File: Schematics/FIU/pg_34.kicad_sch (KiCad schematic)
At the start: 17 parts, among them U3501 F04, U3502 F04, U3503 F04, U3504 F04, U3505 F04, U3506 F04, U3507 F283, U3508 F02, U3509 F02, U3510 F02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

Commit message: Align to grid
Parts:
- removed U3501, U3502, U3503, U3504, U3505, U3506, U3512, U3514: F04, symbol r1000:F04
- removed U3507: F283, symbol r1000:F283
- removed U3508, U3509, U3510, U3511, U3517: F02, symbol r1000:F02
- removed U3513: F181, symbol r1000:F181
- removed U3515, U3516: F157, symbol r1000:F157
- added U (x2): (no value), symbol r1000:F157
- added U (x8): (no value), symbol r1000:F04
- added U (x5): (no value), symbol r1000:F02
- added U: (no value), symbol r1000:F181
- added U: (no value), symbol r1000:F283
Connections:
- net EBIT0: now also U.11 (Y1)
- net EBIT1: now also U.10 (Y2)
- net EBIT2: now also U.9 (Y3)
- net EBIT~3: now also U.3 (Q)
- net EBIT~4: now also U.3 (Q)
- net EBIT~5: now also U.3 (Q)
- net EBIT~6: now also U.3 (Q)
- net LENGTH_ONE0: now also U.1 (D0), U.22 (B2)
- net LENGTH_ONE1: now also U.1 (B3), U.1 (D0)
- net LENGTH_ONE2: now also U.1 (D0), U.11 (B0)
- net LENGTH_ONE3: now also U.1 (D0), U.15 (B1)
- net LENGTH_ONE4: now also U.1 (D0), U.2 (B2)
- net LENGTH_ONE5: now also U.1 (D0), U.6 (B3)
- net LENGTH_ONE~0: now also U.11 (A2), U.2 (Q)
- net LENGTH_ONE~1: now also U.14 (A3), U.2 (Q)
- net LENGTH_ONE~2: now also U.2 (A0), U.2 (Q)
- net LENGTH_ONE~3: now also U.2 (Q), U.5 (A1)
- net LENGTH_ONE~4: now also U.11 (A2), U.2 (Q)
- net LENGTH_ONE~5: now also U.14 (A3), U.2 (Q)
- net OFFSET0.B0: now also U.21 (A1), U.3 (B0), U.6 (B1)
- net OFFSET1: now also U.10 (B2), U.23 (A2)
- net OFFSET2: now also U.13 (B3), U.2 (A3)
- net OFFSET3: now also U.12 (A0), U.3 (B0)
- net OFFSET4: now also U.14 (A1), U.6 (B1)
- net OFFSET5: now also U.10 (B2), U.3 (A2)
- net OFFSET6: now also U.13 (B3), U.5 (A3)
- net OP_SEL0: now also U.1 (S), U.1 (S), U.2 (D1)
- net OP_SEL1: now also U.1 (D0), U.6 (S3)
- net OP_SEL~1: now also U.1 (D0), U.1 (D0), U.1 (D0), U.2 (D1), U.2 (D1), U.2 (Q), U.4 (S1), U.8 (M)
- net PD: now also U.18 (B0), U.19 (A0), U.20 (B1), U.5 (S2), U.7 (CI)
- net PU: now also U.2 (A0), U.3 (S0), U.5 (A1)
- net SBIT0.B0: now also U.4 (Y0)
- net SBIT0.B1: now also U.7 (Y1)
- net SBIT1: now also U.9 (Y2)
- net SBIT2: now also U.12 (Y3)
- net SBIT3: now also U.4 (Y0)
- net SBIT4: now also U.7 (Y1)
- net SBIT5: now also U.9 (Y2)
- net SBIT6: now also U.12 (Y3)
- new net: U.15 (E), U.15 (E), U.3 (Q)
- new net: U.1 (D0), U.4 (Y3)
- new net: U.2 (Q), U.7 (CI)
- new net: U.13 (Y1), U.2 (D1)
- new net: U.10 (Y0), U.2 (D1)
- new net: U.1 (D0), U.9 (CO)
- new net: U.1 (D0), U.1 (Y2)

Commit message: FIU: dedup, clocks, dfsm
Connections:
- net OFFSET0.B0 renamed OFFSET0
- net SBIT0.B0: no longer names the net of U.4 (Y0)
- net SBIT0.B1 renamed SBIT0
- no-connect marks 5 -> 6
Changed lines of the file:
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@@
   (no_connect (at 436.88 149.86))
   (no_connect (at 436.88 144.78))
+  (no_connect (at 187.96 96.52))
   (bus_entry (at 520.7 251.46) (size -2.54 2.54)
     (stroke (width 0) (type default))
@@
     (stroke (width 0) (type default))
   )
+  (bus_entry (at 251.46 104.14) (size -2.54 2.54)
+    (stroke (width 0) (type default))
+  )
   (bus_entry (at 81.28 218.44) (size 2.54 2.54)
     (stroke (width 0) (type default))
@@
     (stroke (width 0) (type default))
   )
-  (bus (pts (xy 251.46 111.76) (xy 259.08 111.76))
+  (bus (pts (xy 251.46 101.6) (xy 259.08 101.6))
     (stroke (width 0) (type default))
   )
@@
     (stroke (width 0) (type default))
   )
-  (wire (pts (xy 187.96 96.52) (xy 248.92 96.52))
-    (stroke (width 0) (type default))
-  )
   (bus (pts (xy 73.66 327.66) (xy 73.66 342.9))
     (stroke (width 0) (type default))
@@
     (stroke (width 0) (type default))
   )
-  (bus (pts (xy 251.46 111.76) (xy 251.46 114.3))
+  (bus (pts (xy 251.46 101.6) (xy 251.46 104.14))
     (stroke (width 0) (type default))
   )
@@
     (stroke (width 0) (type default))
   )
+  (bus (pts (xy 251.46 104.14) (xy 251.46 114.3))
+    (stroke (width 0) (type default))
+  )
   (wire (pts (xy 327.66 165.1) (xy 388.62 165.1))
     (stroke (width 0) (type default))
@@
     (effects (font (size 2.54 2.54)) (justify left bottom))
   )
+  (label "SBIT0" (at 215.9 106.68 0) (fields_autoplaced)
+    (effects (font (size 2.54 2.54)) (justify left bottom))
+  )
   (label "LENGTH_ONE~2" (at 137.16 314.96 0) (fields_autoplaced)
     (effects (font (size 2.54 2.54)) (justify left bottom))
   )
-  (label "OFFSET0.B0" (at 337.82 139.7 0) (fields_autoplaced)
+  (label "OFFSET0" (at 337.82 139.7 0) (fields_autoplaced)
     (effects (font (size 2.54 2.54)) (justify left bottom))
   )
@@
     )
   )
-  (global_label "SBIT0.B0" (shape output) (at 248.92 96.52 0) (fields_autoplaced)
-    (effects (font (size 2.54 2.54)) (justify left))
-    (property "Intersheet References" "${INTERSHEET_REFS}" (id 0) (at 270.4374 96.3613 0)
-      (effects (font (size 1.905 1.905)) (justify left))
-    )
-  )
-  (global_label "OFFSET0.B0" (shape input) (at 68.58 119.38 180) (fields_autoplaced)
+  (global_label "OFFSET0" (shape input) (at 68.58 119.38 180) (fields_autoplaced)
     (effects (font (size 2.54 2.54)) (justify right))
     (property "Intersheet References" "${INTERSHEET_REFS}" (id 0) (at 41.4988 119.2213 0)
       (effects (font (size 1.905 1.905)) (justify right))
-    )
-  )
-  (global_label "SBIT0.B1" (shape output) (at 248.92 106.68 0) (fields_autoplaced)
-    (effects (font (size 2.54 2.54)) (justify left))
-    (property "Intersheet References" "${INTERSHEET_REFS}" (id 0) (at 270.4374 106.5213 0)
-      (effects (font (size 1.905 1.905)) (justify left))
     )
   )
@@
     )
   )
-  (global_label "SBIT[1..6]" (shape output) (at 259.08 111.76 0) (fields_autoplaced)
+  (global_label "SBIT[0..6]" (shape output) (at 259.08 101.6 0) (fields_autoplaced)
     (effects (font (size 2.54 2.54)) (justify left))
-    (property "Intersheet References" "${INTERSHEET_REFS}" (id 0) (at 282.6536 111.6013 0)
+    (property "Intersheet References" "${INTERSHEET_REFS}" (id 0) (at 283.3202 101.6 0)
       (effects (font (size 1.905 1.905)) (justify left))
     )

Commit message: FIU: tested to 6.07s (rc019)
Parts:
- removed U (x2): (no value), symbol r1000:F157
- added U: XMUX7, symbol r1000:XMUX7
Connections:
- net LENGTH_ONE~0: now also U.3 (A1)
- net LENGTH_ONE~1: now also U.5 (A2)
- net LENGTH_ONE~2: now also U.7 (A3)
- net LENGTH_ONE~3: now also U.9 (A4)
- net LENGTH_ONE~4: now also U.10 (A5)
- net LENGTH_ONE~5: now also U.11 (A6)
- net OFFSET0: now also U.12 (B0)
- net OFFSET1: now also U.14 (B1)
- net OFFSET2: now also U.16 (B2)
- net OFFSET3: now also U.18 (B3)
- net OFFSET4: now also U.20 (B4)
- net OFFSET5: now also U.22 (B5)
- net OFFSET6: now also U.24 (B6)
- net OP_SEL0: now also U.4 (S)
- net PD: now also U.8 (OE)
- net PU: now also U.1 (A0)
- net SBIT0: now also U.13 (Y0)
- net SBIT1: now also U.15 (Y1)
- net SBIT2: now also U.17 (Y2)
- net SBIT3: now also U.19 (Y3)
- net SBIT4: now also U.21 (Y4)
- net SBIT5: now also U.23 (Y5)
- net SBIT6: now also U.25 (Y6)
- net at U.3 (Q): now also U.6 (E)

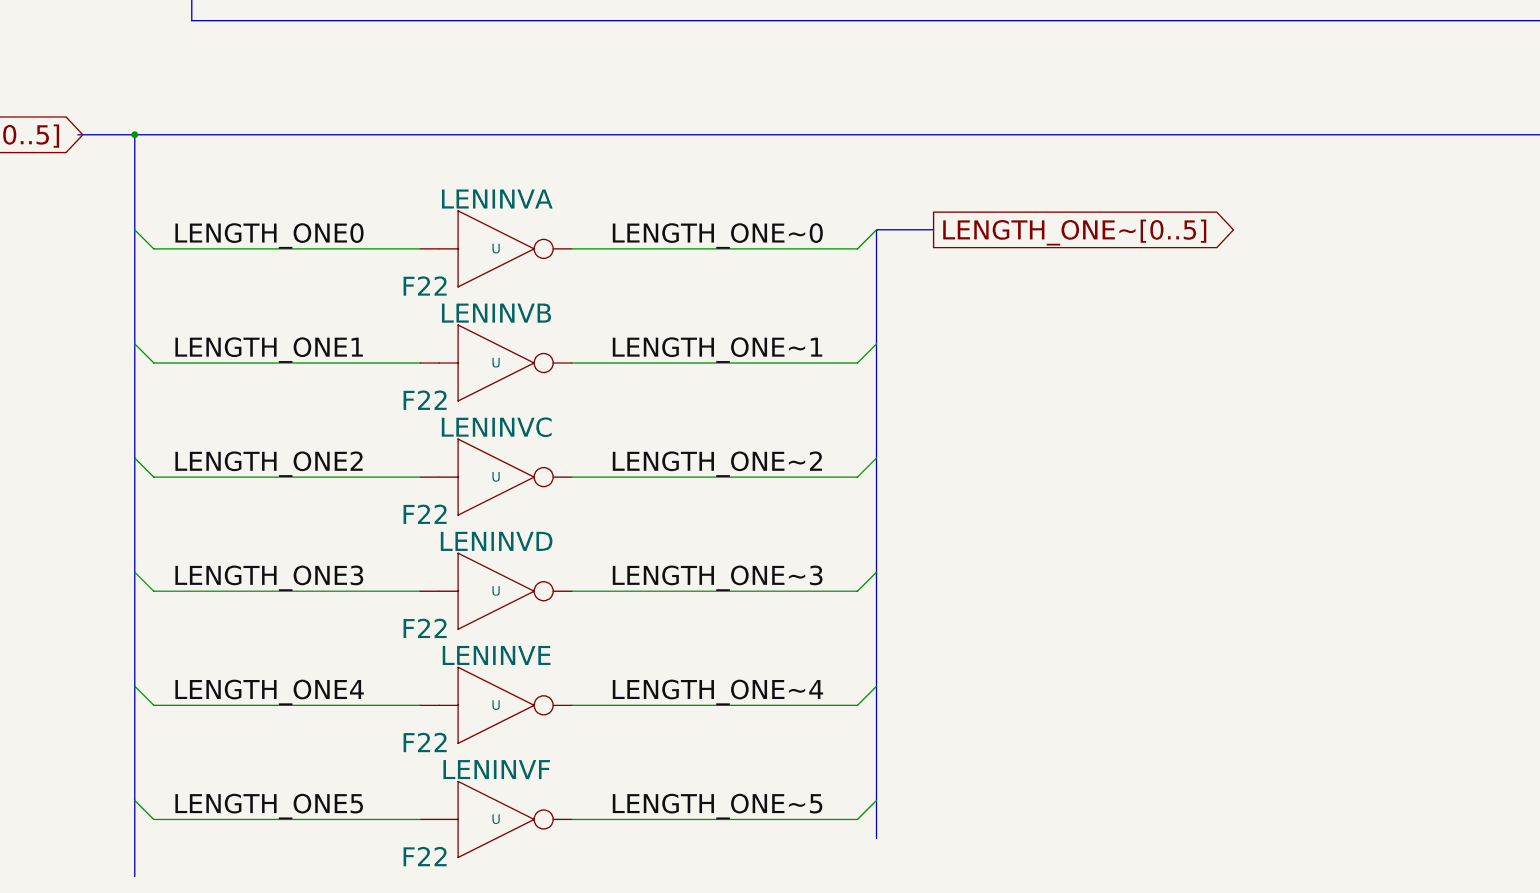
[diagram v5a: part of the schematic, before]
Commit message: FIU tested to 21.22 seconds (rm089)
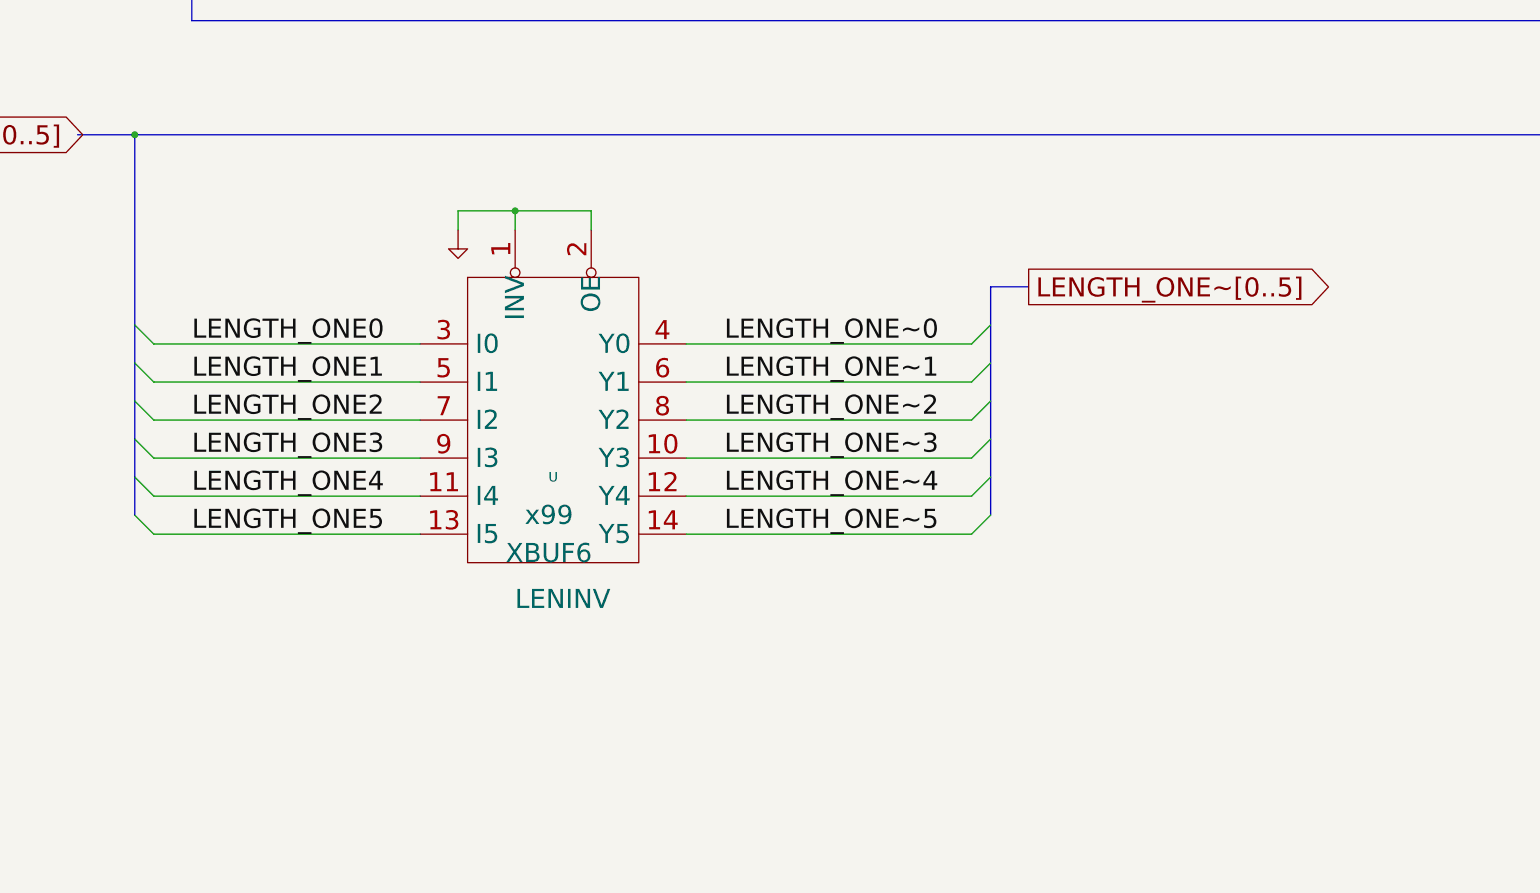
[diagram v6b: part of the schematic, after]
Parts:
- removed U (x6): (no value), symbol r1000:F04
- added U: XBUF6, symbol r1000:XBUF6
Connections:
- net LENGTH_ONE0: now also U.3 (I0)
- net LENGTH_ONE1: now also U.5 (I1)
- net LENGTH_ONE2: now also U.7 (I2)
- net LENGTH_ONE3: now also U.9 (I3)
- net LENGTH_ONE4: now also U.11 (I4)
- net LENGTH_ONE5: now also U.13 (I5)
- net LENGTH_ONE~0: now also U.4 (Y0)
- net LENGTH_ONE~1: now also U.6 (Y1)
- net LENGTH_ONE~2: now also U.8 (Y2)
- net LENGTH_ONE~3: now also U.10 (Y3)
- net LENGTH_ONE~4: now also U.12 (Y4)
- net LENGTH_ONE~5: now also U.14 (Y5)
- net PD: now also U.1 (INV), U.2 (OE)

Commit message: Eliminate empty pages
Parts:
- U3507: renamed from U; value (none) -> F283
- U3508, U3509, U3510, U3511, U3517: renamed from U; value (none) -> F02
- U3512, U3514: renamed from U; value (none) -> F04
- U3513: renamed from U; value (none) -> F181
- renumbered U to U82, U to U84

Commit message: Schematics for run rr026
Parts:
- added U3401: F02, symbol r1000:F02
- added U80: XADD8, symbol r1000:XADD8
- added U81: XMUX6, symbol r1000:XMUX6
- added U83: XSUB8, symbol r1000:XSUB8
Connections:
- net LENGTH_ONE0: now also U80.15 (B2)
- net LENGTH_ONE1: now also U80.17 (B3)
- net LENGTH_ONE2: now also U80.19 (B4)
- net LENGTH_ONE3: now also U80.21 (B5)
- net LENGTH_ONE4: now also U80.23 (B6)
- net LENGTH_ONE5: now also U80.25 (B7)
- net LENGTH_ONE~0: now also U83.15 (B2)
- net LENGTH_ONE~1: now also U83.17 (B3)
- net LENGTH_ONE~2: now also U83.19 (B4)
- net LENGTH_ONE~3: now also U83.21 (B5)
- net LENGTH_ONE~4: now also U83.23 (B6)
- net LENGTH_ONE~5: now also U83.25 (B7)
- net OFFSET0: now also U80.4 (A1), U83.4 (A1)
- net OFFSET1: now also U80.5 (A2), U83.5 (A2)
- net OFFSET2: now also U80.6 (A3), U83.6 (A3)
- net OFFSET3: now also U80.7 (A4), U83.7 (A4)
- net OFFSET4: now also U80.8 (A5), U83.8 (A5)
- net OFFSET5: now also U80.9 (A6), U83.9 (A6)
- net OFFSET6: now also U80.10 (A7), U83.10 (A7)
- net OP_SEL0: now also U3401.1 (D0)
- net OP_SEL1: now also U3401.2 (D1)
- net PD: now also U80.11 (B0), U80.13 (B1), U80.3 (A0), U81.6 (E), U81.8 (OE), U83.3 (A0)
- net PU: now also U80.1 (CI), U83.11 (B0), U83.13 (B1); no longer U3513.3 (S0)
- new net EXTRACT: U3401.3 (Q), U81.4 (S)
- new net EXTRACT_ROT1: U81.11 (B0), U83.16 (Y2)
- new net EXTRACT_ROT2: U81.13 (B1), U83.18 (Y3)
- new net EXTRACT_ROT3: U81.15 (B2), U83.20 (Y4)
- new net EXTRACT_ROT4: U81.17 (B3), U83.22 (Y5)
- new net EXTRACT_ROT5: U81.19 (B4), U83.24 (Y6)
- new net EXTRACT_ROT6: U81.21 (B5), U83.26 (Y7)
- new net INSERT_ROT1: U80.16 (Y2), U81.1 (A0)
- new net INSERT_ROT2: U80.18 (Y3), U81.3 (A1)
- new net INSERT_ROT3: U80.20 (Y4), U81.5 (A2)
- new net INSERT_ROT4: U80.22 (Y5), U81.7 (A3)
- new net INSERT_ROT5: U80.24 (Y6), U81.9 (A4)
- new net INSERT_ROT6: U80.26 (Y7), U81.10 (A5)
- new net ROT_AMT1: U81.12 (Y0)
- new net ROT_AMT2: U81.14 (Y1)
- new net ROT_AMT3: U81.16 (Y2)
- new net ROT_AMT4: U81.18 (Y3)
- new net ROT_AMT5: U81.20 (Y4)
- new net ROT_AMT6: U81.22 (Y5)
- no-connect marks 6 -> 15
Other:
- moved on the sheet: U3507, U3508, U3509, U3510, U3511, U3512, U3513, U3514, U3517, U82, U84
